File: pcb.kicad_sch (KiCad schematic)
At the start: 76 parts

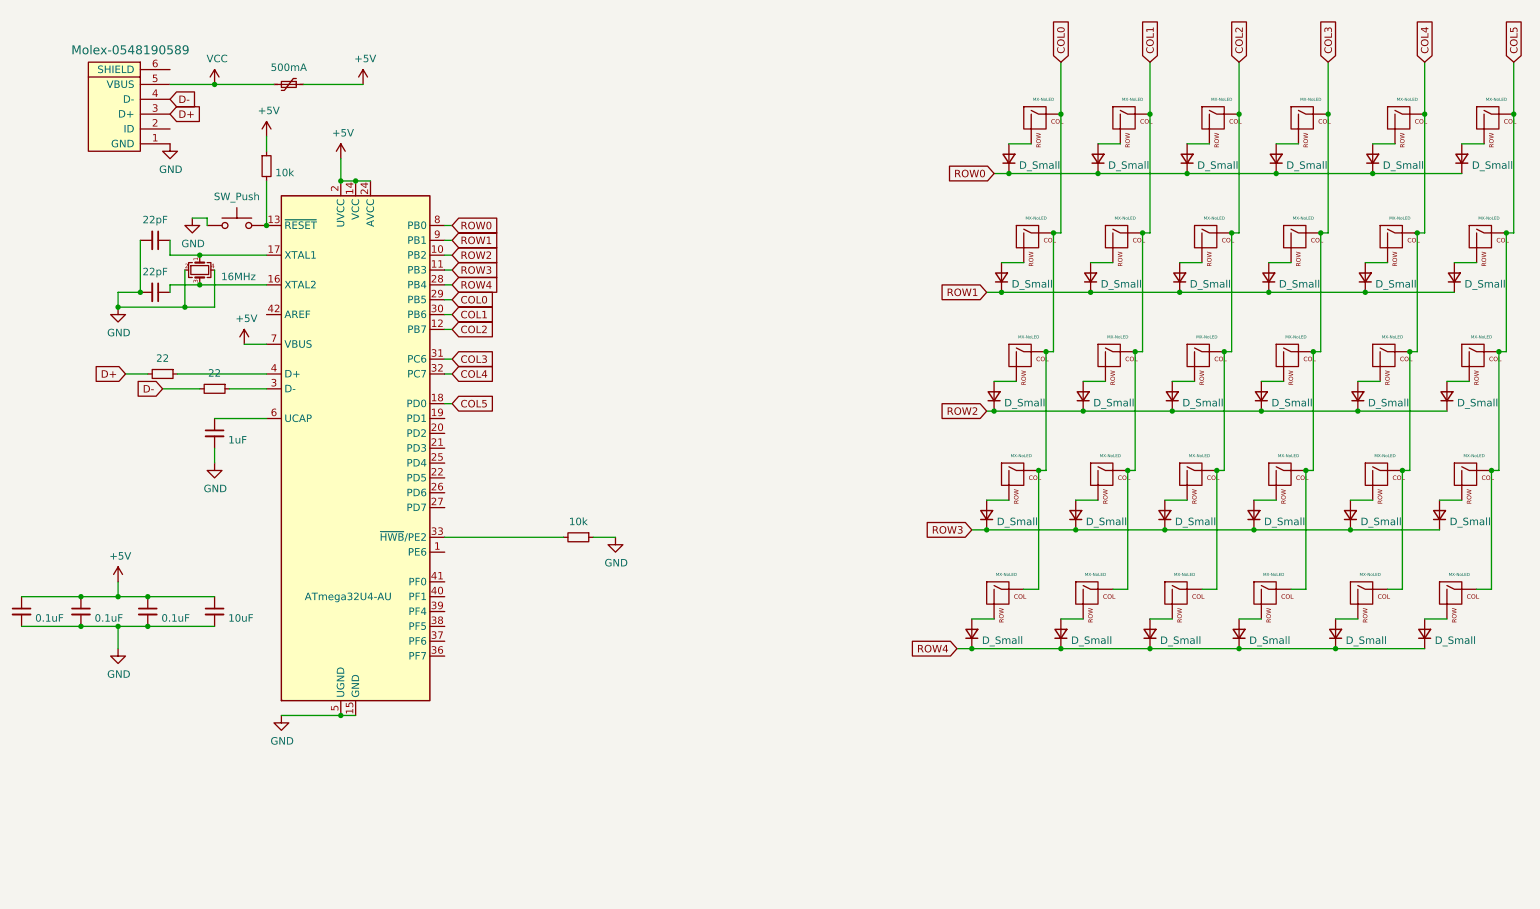
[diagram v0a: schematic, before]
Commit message: Cleaned PCB
Added hotswap, started new trace routes
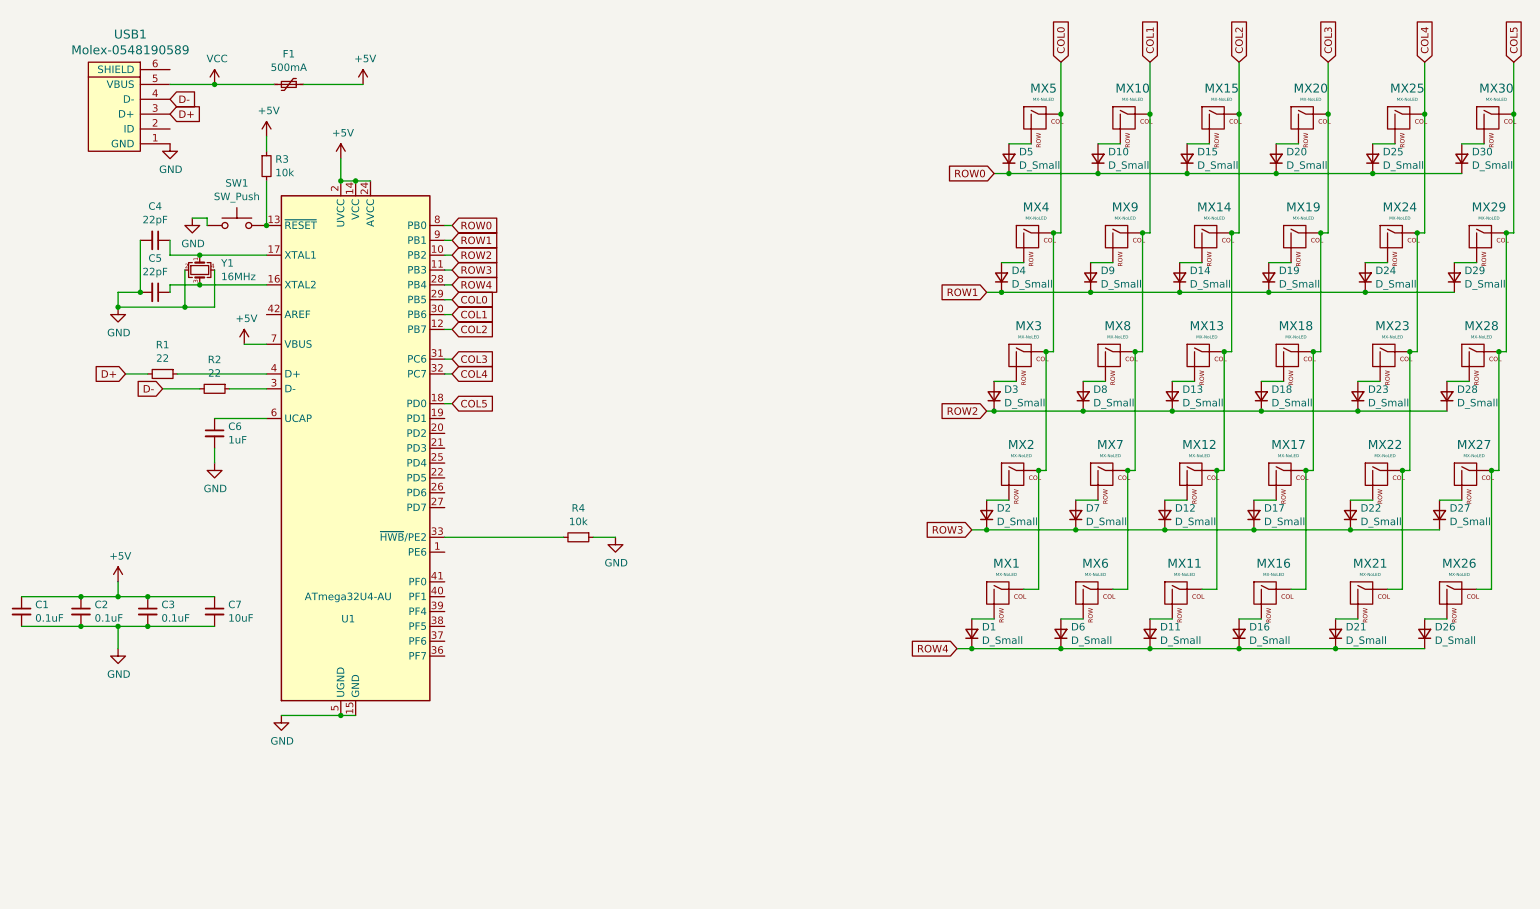
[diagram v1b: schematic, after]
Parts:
- MX1, MX10, MX11, MX12, MX13, MX14, MX15, MX16, MX17, MX18, MX19, MX20, MX22, MX23, MX24, MX25, MX26, MX27, MX28, MX29, MX30, MX5, MX6, MX7, MX8, MX9: renamed from ?; footprint MX_Alps_Hybrid_Included:MX-1U-NoLED -> MXHotswaps:MX-Hotswap-1U
- MX2, MX21: renamed from ?; footprint MX_Alps_Hybrid_Included:MX-2U-NoLED -> MXHotswaps:MX-Hotswap-2U
- MX3: renamed from ?; footprint MX_Alps_Hybrid_Included:MX-1.75U-NoLED -> MXHotswaps:MX-Hotswap-1.75U
- MX4: renamed from ?; footprint MX_Alps_Hybrid_Included:MX-1.5U-NoLED -> MXHotswaps:MX-Hotswap-1.5U
- gave numbers to parts that had none: 46

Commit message: V0.2
Replaced Footprint. Trace Routes (almost) done
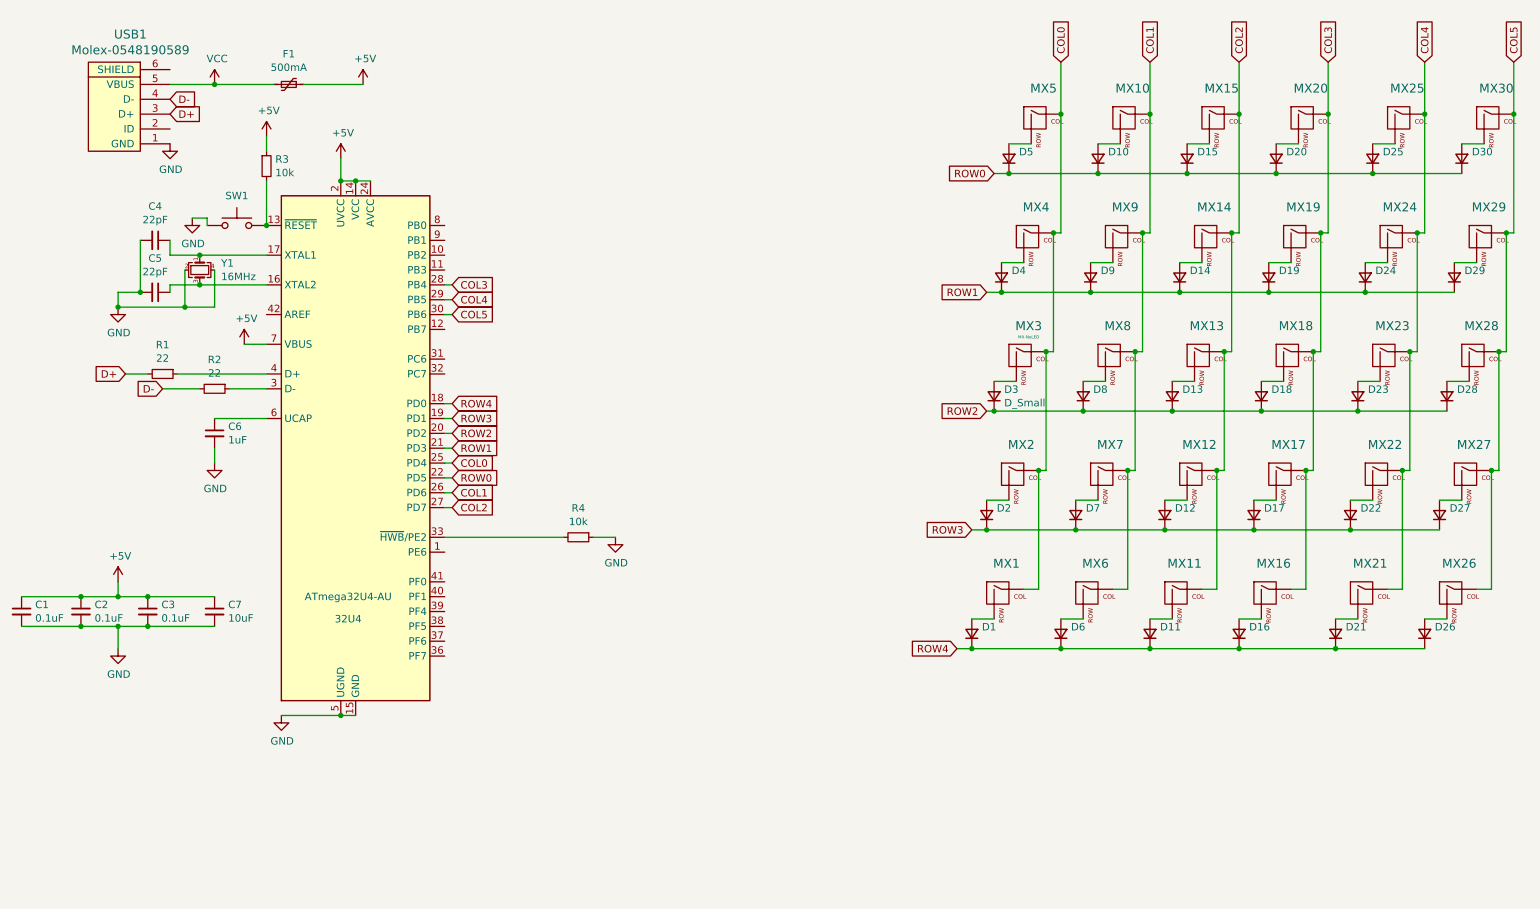
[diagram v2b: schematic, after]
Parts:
- MX1, MX10, MX11, MX12, MX13, MX14, MX15, MX16, MX17, MX18, MX19, MX20, MX22, MX23, MX24, MX25, MX26, MX27, MX28, MX29, MX30, MX5, MX6, MX7, MX8, MX9: footprint MXHotswaps:MX-Hotswap-1U -> MXHotswaps:MXOnly-1U-Hotswap-Modified
- MX2, MX21: footprint MXHotswaps:MX-Hotswap-2U -> MXHotswaps:MXOnly-1U-Hotswap-Modified
- MX3: footprint MXHotswaps:MX-Hotswap-1.75U -> MXHotswaps:MXOnly-1U-Hotswap-Modified
- MX4: footprint MXHotswaps:MX-Hotswap-1.5U -> MXHotswaps:MXOnly-1U-Hotswap-Modified
- renumbered U1 to 32U4
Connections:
- net COL0: now also 32U4.25 (PD4); no longer 32U4.29 (PB5)
- net COL1: now also 32U4.26 (PD6); no longer 32U4.30 (PB6)
- net COL2: now also 32U4.27 (PD7); no longer 32U4.12 (PB7)
- net COL3: now also 32U4.28 (PB4); no longer 32U4.31 (PC6)
- net COL4: now also 32U4.29 (PB5); no longer 32U4.32 (PC7)
- net COL5: now also 32U4.30 (PB6); no longer 32U4.18 (PD0)
- net ROW0: now also 32U4.22 (PD5); no longer 32U4.8 (PB0)
- net ROW1: now also 32U4.21 (PD3); no longer 32U4.9 (PB1)
- net ROW2: now also 32U4.20 (PD2); no longer 32U4.10 (PB2)
- net ROW3: now also 32U4.19 (PD1); no longer 32U4.11 (PB3)
- net ROW4: now also 32U4.18 (PD0); no longer 32U4.28 (PB4)

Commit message: Spaghetti Junction
Yummm
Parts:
- added C8, C9: 0.1uF, Capacitor_SMD:C_0805_2012Metric, symbol Device:C_Small
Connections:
- net +5V: now also C8.1, C9.1
- net GND: now also C8.2, C9.2
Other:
- moved on the sheet: C1, C2, C3, C7
